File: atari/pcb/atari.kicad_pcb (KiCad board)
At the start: 2 copper layers, 228 x 85.7 mm, 173 parts, among them U1 NiceNano

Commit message: moved diodes in; cleanup; fixed fill
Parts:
- Bat+, BatGND, PowSw1, PowSw2: footprint Connector_Wire:SolderWire-1sqmm_1x01_D1.4mm_OD2.7mm -> Connector_Wire:SolderWire-0.5sqmm_1x01_D0.9mm_OD2.1mm
- U1: value NiceNano -> Nice_Nano
- moved D1_1 52.9 mm to (85.6, 37.1)
- moved D1_2 40.4 mm to (95.5, 36.6)
- moved D1_3 39.2 mm to (105.4, 37.1)
- moved D1_4 32.5 mm to (116.8, 37.1)
- moved D1_12 30.5 mm to (204.5, 37.1)
- moved D1_5 25.4 mm to (127.0, 37.3)
- moved D1_6 20.5 mm to (139.2, 37.1)
- moved D1_11 19.1 mm to (193.5, 37.1)
- moved D1_10 18.5 mm to (183.4, 37.1)
- moved D1_9 18.2 mm to (172.7, 37.1)
- moved D1_7 17.1 mm to (150.4, 37.1)
- moved D1_8 16.9 mm to (161.5, 37.1)
- moved D2_1 11.6 mm to (60.2, 37.1), turned to 0 degrees
- moved D2_6 1.12 mm to (140.4, 39.8)
- turned Bat+ to 90 degrees
- renumbered Reset to Reset1
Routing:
- net r1: track 247.6 -> 152.6 mm
- net r3: track 291.3 -> 211.4 mm
- net C10: track 266.1 -> 339.4 mm
- net Net-(D2_1-A): track 15.8 -> 79.7 mm
- net Net-(D1_1-A): track 17.9 -> 75.1 mm
- net Net-(D1_12-A): track 7.75 -> 57.9 mm
- net Net-(D1_2-A): track 21.1 -> 65.6 mm
- net Net-(D1_4-A): track 15.6 -> 44.5 mm
- net c11: track 272.7 -> 297.4 mm
- net Net-(D1_5-A): track 15.6 -> 38.5 mm
- net r2: track 178.2 -> 156.5 mm
- net Net-(D1_3-A): track 23.7 -> 41.3 mm
- net c3: track 235.1 -> 218.6 mm
- net Net-(D1_8-A): track 15.6 -> 30.4 mm
- net c8: track 227.7 -> 242.1 mm
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- added copper zone on B.Cu, net gnd
- added copper zone on F.Cu, net gnd

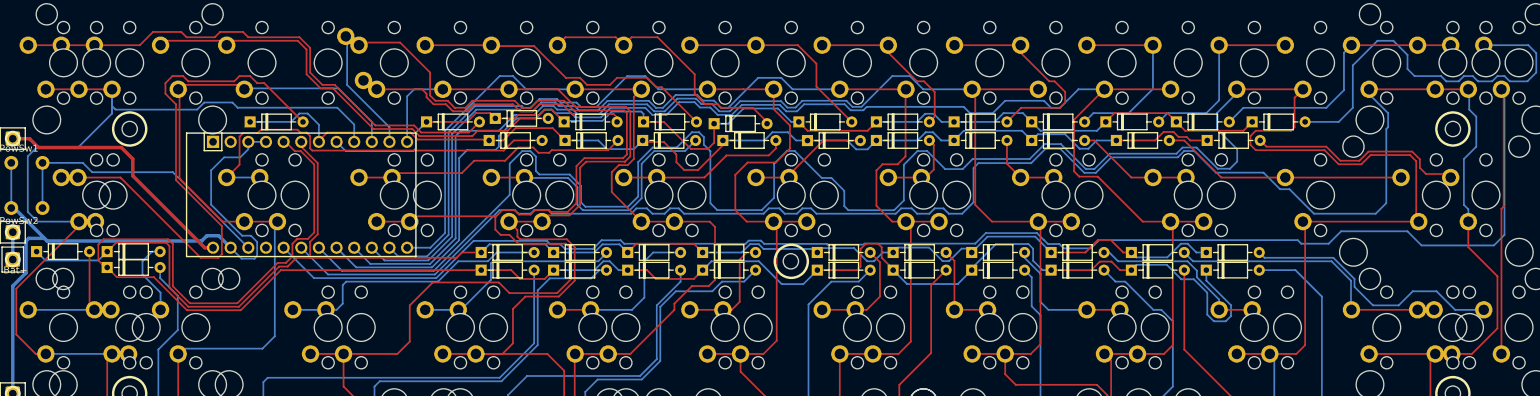
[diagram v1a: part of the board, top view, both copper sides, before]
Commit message: cleanup; fill remaining holes where possible
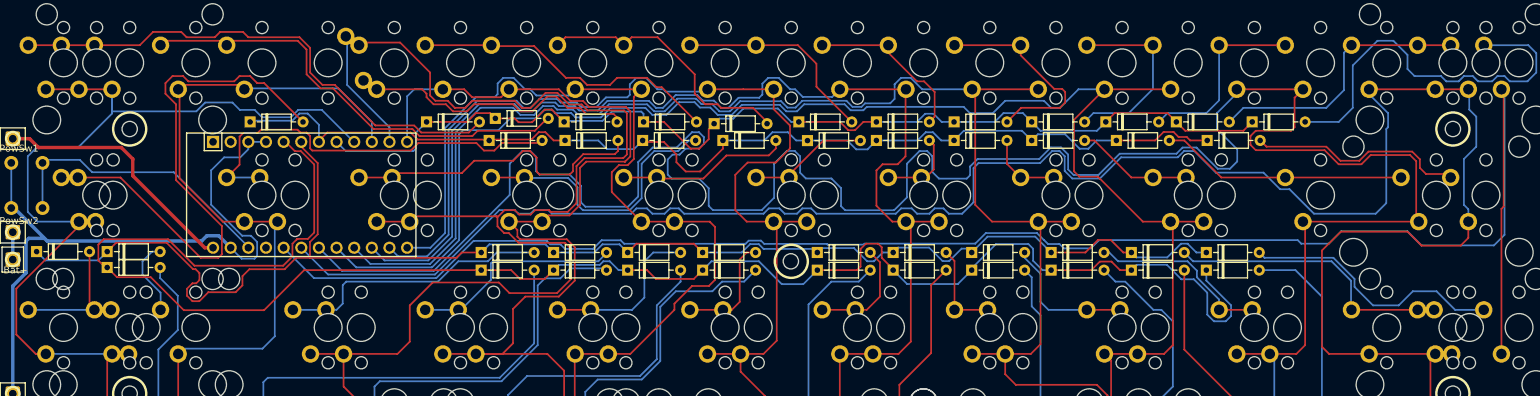
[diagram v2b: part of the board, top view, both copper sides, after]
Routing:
- net c11: track 297.4 -> 320.8 mm
- net C10: track 339.4 -> 354.3 mm
- net r4: track 262.7 -> 254.6 mm
- net Net-(D2_3-A): track 40.1 -> 44.9 mm
- net c7: track 190.2 -> 192.9 mm
- net c8: track 242.1 -> 244.3 mm
- net c6: track 155.2 -> 157.0 mm
- net c5: track 149.7 -> 151.4 mm
- net r3: track 211.4 -> 212.7 mm
- net c9: track 245.0 -> 246.1 mm
- net c4: track 160.9 -> 161.8 mm
- net Net-(D1_3-A): track 41.3 -> 42.3 mm
- net Net-(D2_2-A): track 58.3 -> 59.2 mm
- net Net-(D4_3-A): track 63.4 -> 64.0 mm

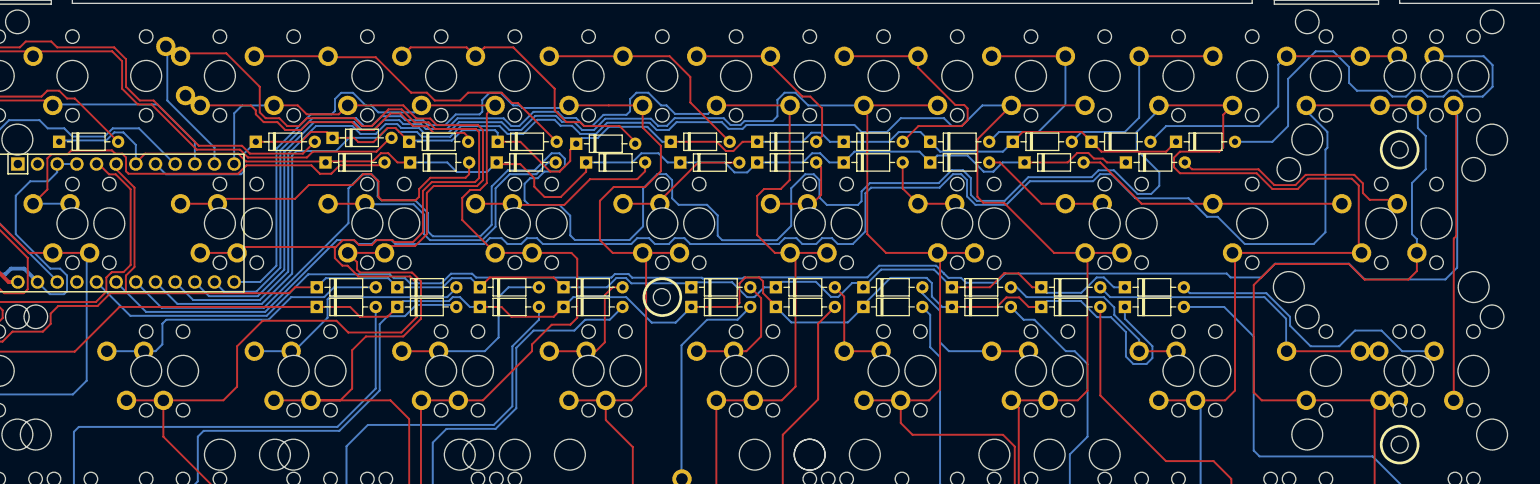
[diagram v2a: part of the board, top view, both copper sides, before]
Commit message: more cleanup; optimizing fill ratio
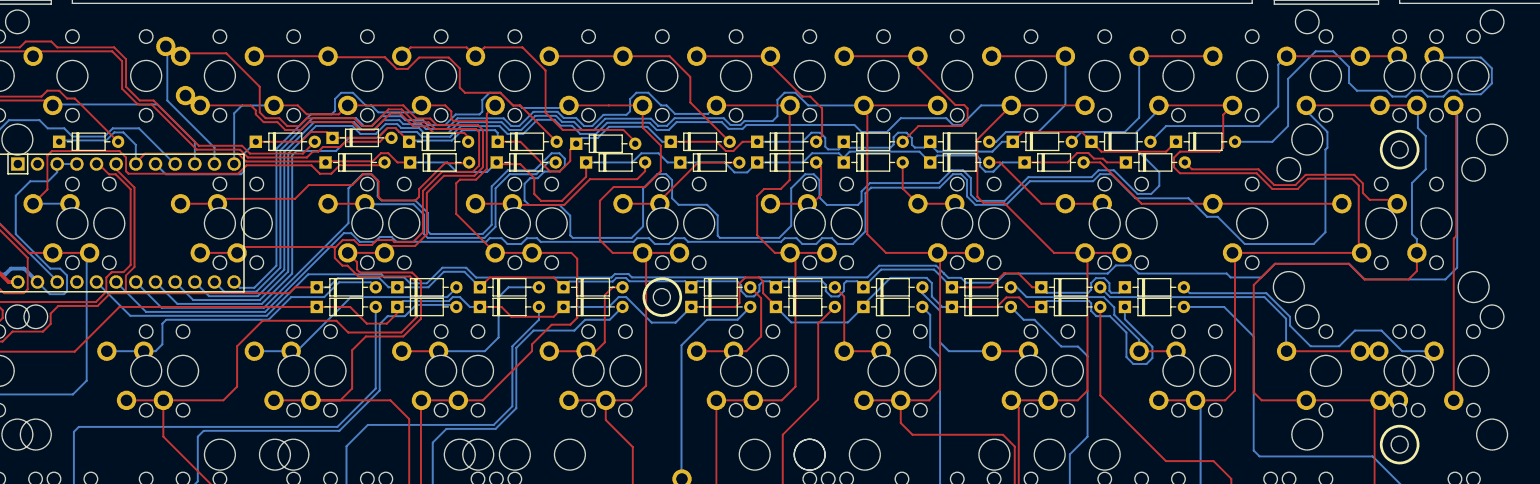
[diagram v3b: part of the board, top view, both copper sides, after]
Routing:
- net r3: track 212.7 -> 217.8 mm
- net r1: track 152.2 -> 155.8 mm
- net r2: track 156.5 -> 159.1 mm
- net c5: track 151.4 -> 153.5 mm
- net Net-(D1_4-A): track 44.5 -> 46.3 mm
- net r4: track 254.6 -> 256.4 mm
- net Net-(D1_5-A): track 38.5 -> 40.1 mm
- net Net-(D3_4-A): track 31.0 -> 29.6 mm
- net c12: track 245.5 -> 246.8 mm
- net c4: track 161.8 -> 160.8 mm
- net c3: track 218.9 -> 218.0 mm
- net Net-(D1_12-A): track 57.9 -> 57.0 mm
- net Net-(D2_3-A): track 44.9 -> 44.1 mm
- net C10: track 354.3 -> 353.6 mm
- net Net-(D4_9-A): track 41.1 -> 41.7 mm
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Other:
- board text added: "TIARTIITIIRTIITRIARTIRTIIARTIR ATIRRIATIRIRTAITIRITRAIRTIARIT AITIREADY ITIRITARIIRARARRAIRT ITITIIRRRATIRRIRIARIITAAITIARI TIRIATIRIRITIRATIRIRAITRIATIIT TAIIRIIRTIARTIIRTIARTIITIIRTII ITARTIAITATARITRTARITARTARIATI IIARIRITIITTIRIARITIRAITIRTITR ATIITIARIIRTIARITIITIRATIARITI IRIRITIRATIRIRAITRIATIITRRITIA"
